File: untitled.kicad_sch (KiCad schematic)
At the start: 28 parts, among them Q1 AO3401A, Q2 AO3401A, Q3 AO3401A, U2 STM32L100RBT6A_LQFP64, U4 RC1587_3V3, U8 LTC4002ES8-4.2

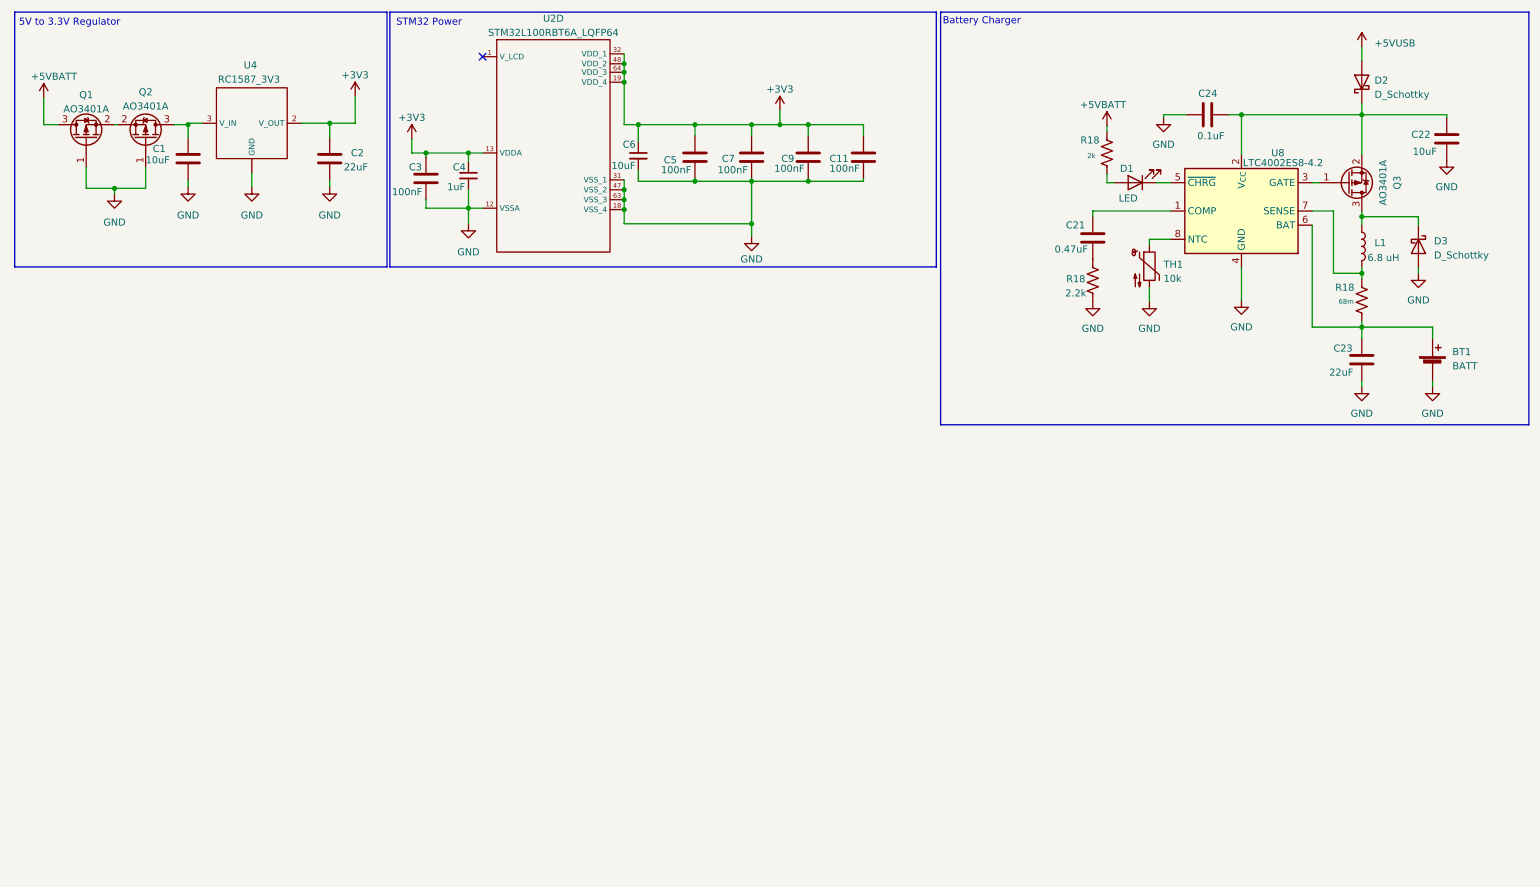
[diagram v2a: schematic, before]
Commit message: Rev 0.3
+ Updated schematic to reflect utilization of USB-B micro instead of USB-C
+ Began initial layout of PCB

- Need to look into eFuse layout, as specified layout recommendation utilizes ground pours
- Need to update SD Card footprint as pads are not linked
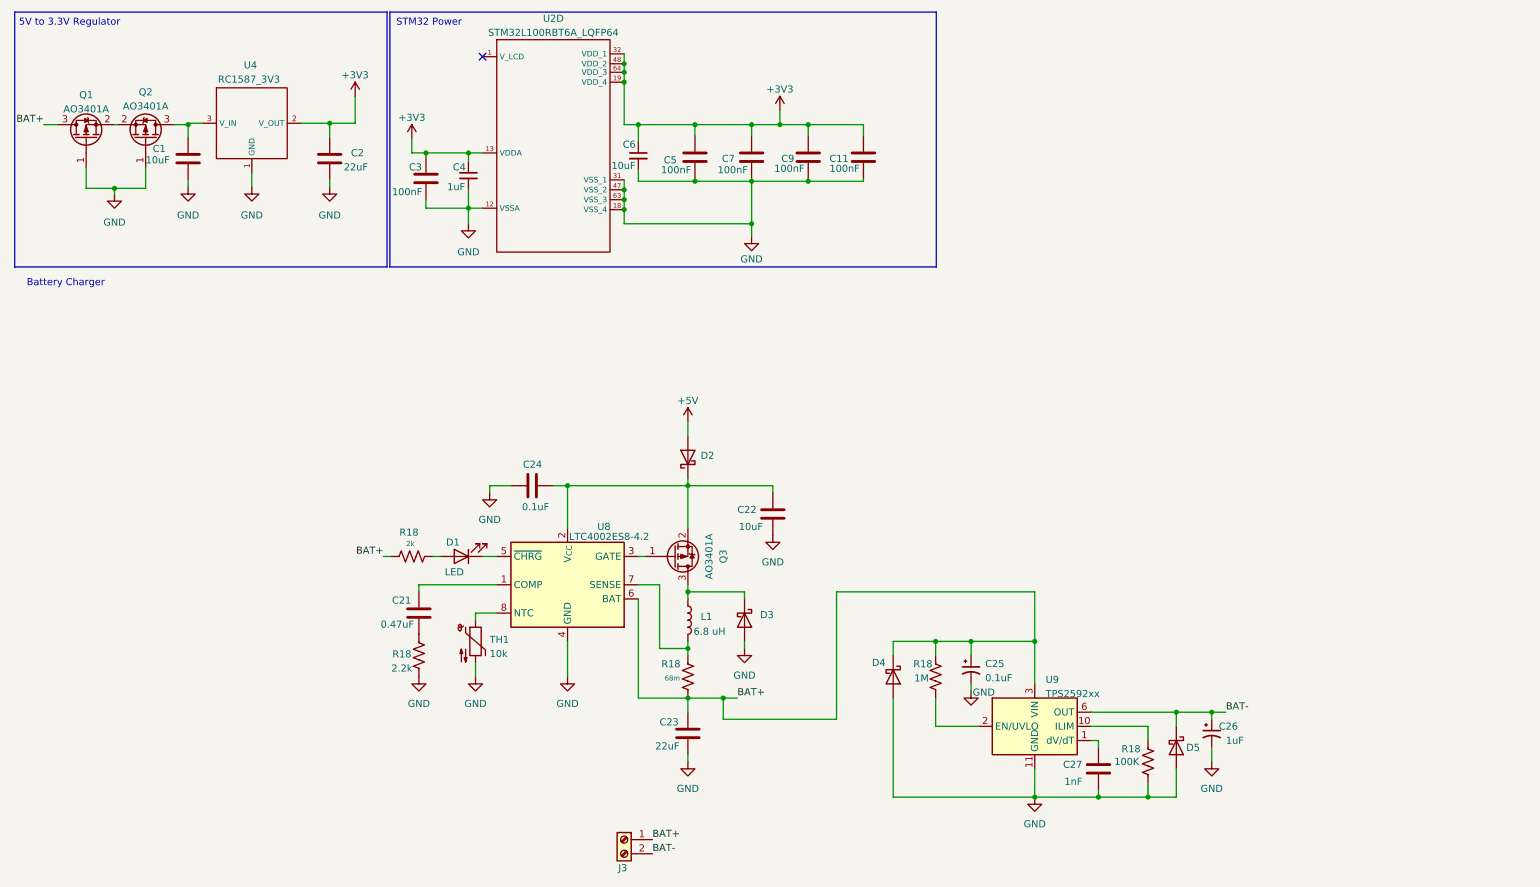
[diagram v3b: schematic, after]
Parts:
- removed BT1: BATT, symbol Device:Battery_Cell
- added C25: 0.1uF, Capacitor_SMD:C_0805_2012Metric, symbol Device:C_Polarized_Small_US
- added C26: 1uF, Capacitor_SMD:C_0805_2012Metric, symbol Device:C_Polarized_Small_US
- added C27: 1nF, Capacitor_SMD:C_0805_2012Metric, symbol Device:C
- added D4, D5: D_Schottky, Diode_SMD:D_0805_2012Metric, symbol Device:D_Schottky
- added J3: Screw_Terminal_01x02, TerminalBlock:TerminalBlock_Altech_AK300-2_P5.00mm, symbol Connector:Screw_Terminal_01x02
- added R18: 1M, Resistor_SMD:R_0805_2012Metric, symbol Device:R_US
- added R18: 100K, Resistor_SMD:R_0805_2012Metric, symbol Device:R_US
- added U9: TPS2592xx, Package_SON:VSON-10-1EP_3x3mm_P0.5mm_EP1.65x2.4mm_ThermalVias, symbol Power_Management:TPS2592xx
- D1: footprint (none) -> LED_SMD:LED_0805_2012Metric
- D2, D3: footprint (none) -> Diode_SMD:D_0805_2012Metric
- L1: footprint (none) -> Inductor_SMD:L_0805_2012Metric
- TH1: footprint (none) -> Resistor_SMD:R_0805_2012Metric
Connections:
- net +BATT is gone; now on net BAT+: R18.2
- net +5V: no longer Q1.3 (D)
- net GND: now also U4.1 (GND), C25.2, C26.2, C27.2, D4.2 (A), D5.2 (A), R18.1, U9.11 (GND); no longer U4. (GND)
- net BAT+: now reaches C23.1, R18.1, U8.6 (BAT)
- net BAT+: now also Q1.3 (D), C25.1, D4.1 (K), J3.1 (Pin_1), R18.2, U9.3 (VIN), U9.4 (VIN), U9.5 (VIN)
- new net: R18.1, U9.2 (EN/UVLO)
- new net: R18.2, U9.10 (ILIM)
- new net: C27.1, U9.1 (dV/dT)
- new net BAT-: C26.1, D5.1 (K), J3.2 (Pin_2), U9.6 (OUT), U9.7 (OUT), U9.8 (OUT)
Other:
- moved on the sheet: C21, C22, C23, C24, D1, D2, D3, L1, Q3, R18, TH1, U8

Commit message: Updated to Rev 1.1
+ Adjusted trace widths to appropriately fit IC pads while supporting wanted current and minimizing vdrop
+ Adjusted edge cuts of PCB to remove unnecessary areas
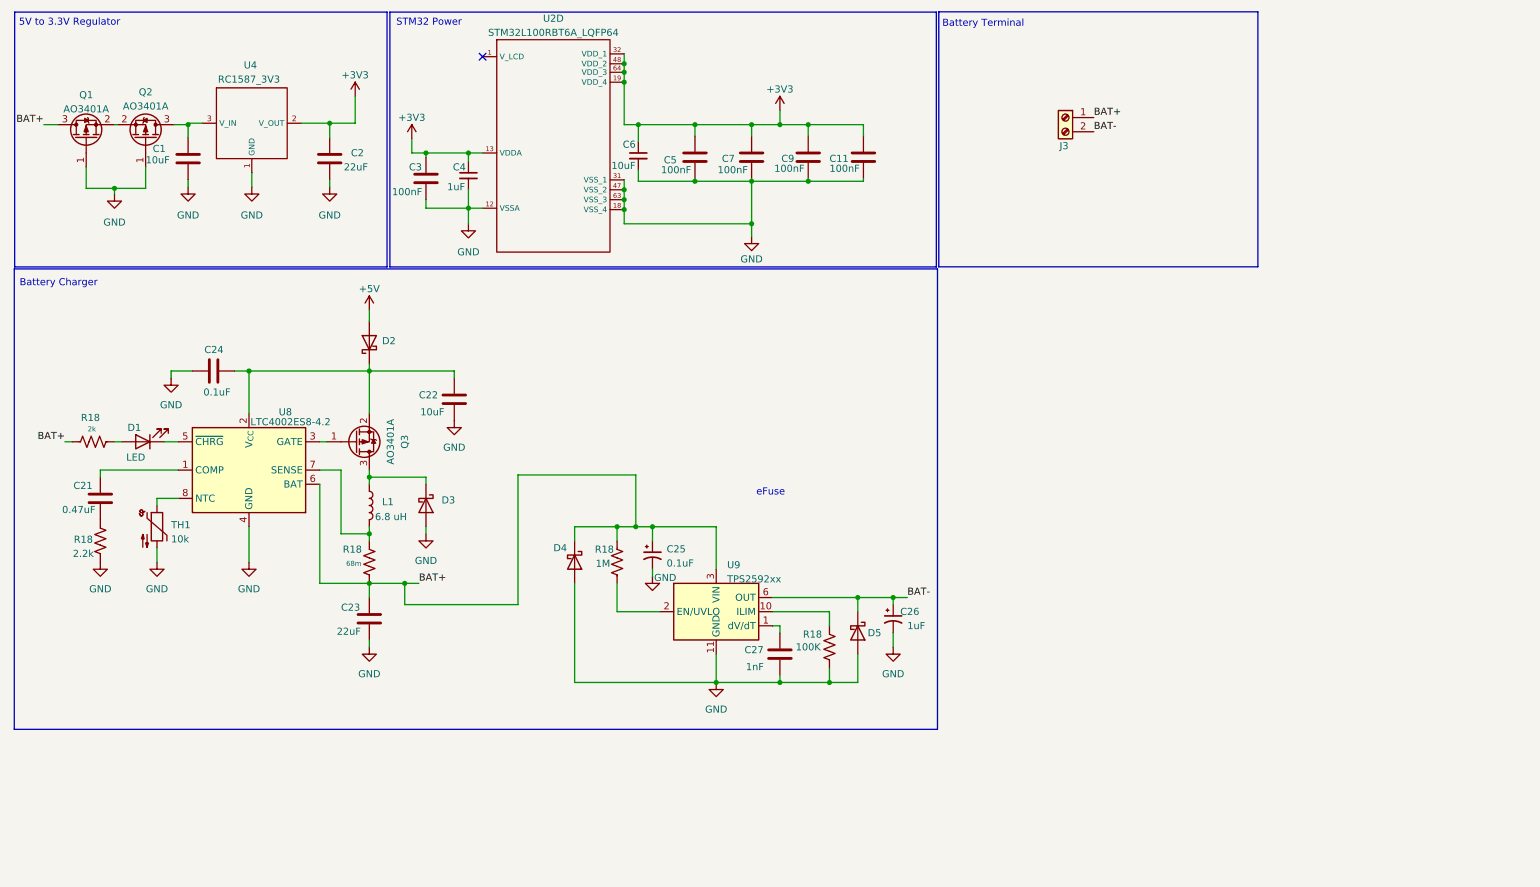
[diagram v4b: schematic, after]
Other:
- note added: "Battery Terminal"
- note added: "eFuse"
- moved on the sheet: C21, C22, C23, C24, C25, C26, C27, D1, D2, D3, D4, D5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

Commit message: Updated Rev 2.0
+ Revamped board to 4 layer with components on both signal layers (top/bottom)
+ Adjusted compactness of components, reducing size by approx 30%
+ Added mounting holes for mounting purposes
- Removed battery, batt charger, eFuse (USB driven only)
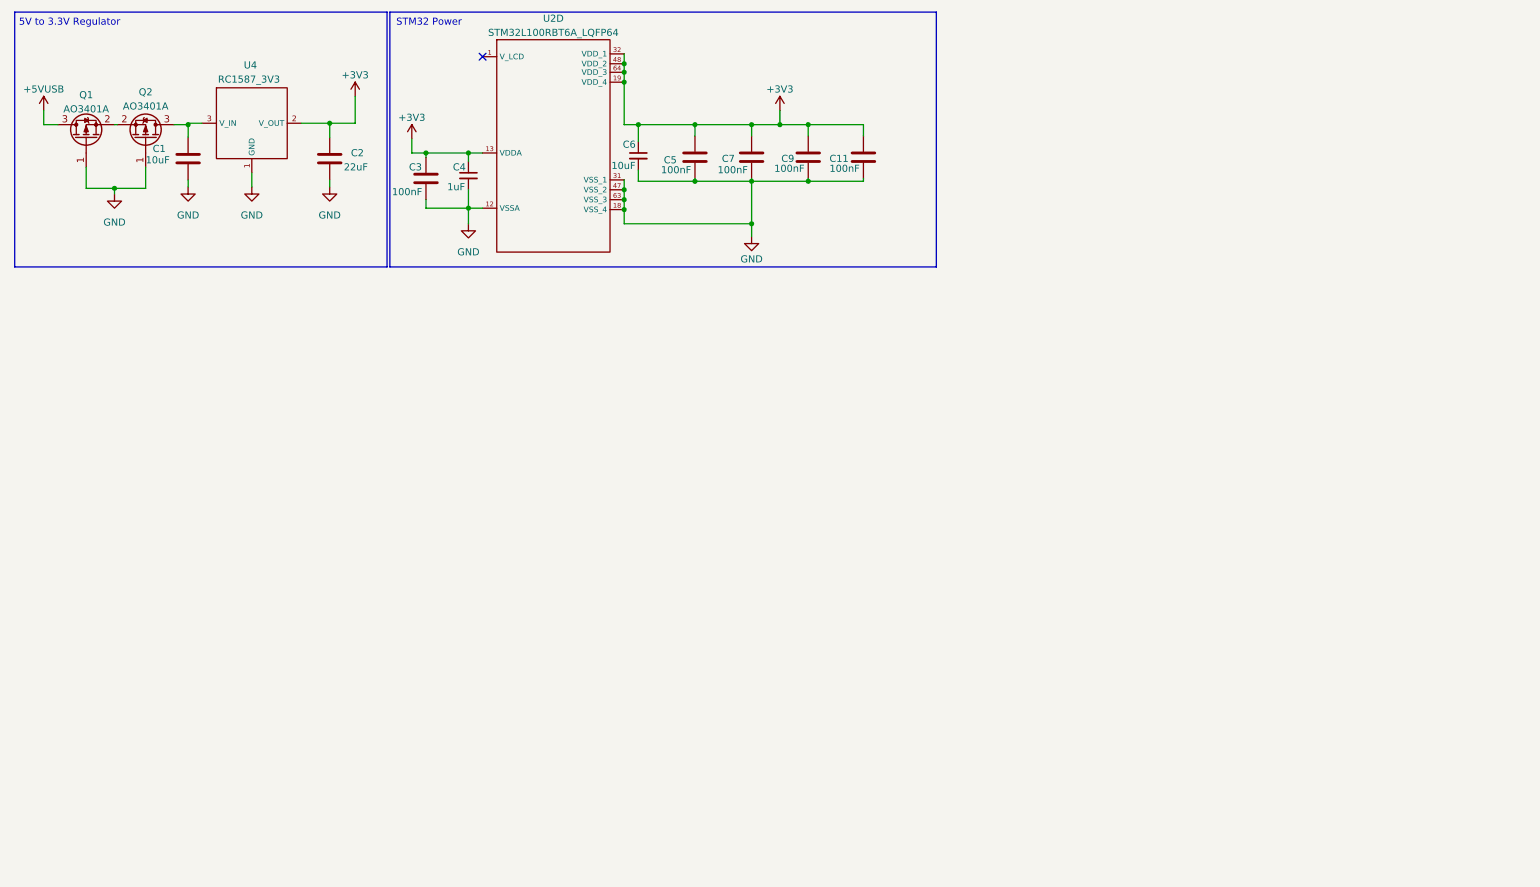
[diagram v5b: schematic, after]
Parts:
- removed C21: 0.47uF, Capacitor_SMD:C_0805_2012Metric, symbol Device:C
- removed C22: 10uF, Capacitor_SMD:C_0805_2012Metric, symbol Device:C
- removed C23: 22uF, Capacitor_SMD:C_0805_2012Metric, symbol Device:C
- removed C24: 0.1uF, Capacitor_SMD:C_0805_2012Metric, symbol Device:C
- removed C25: 0.1uF, Capacitor_SMD:C_0805_2012Metric, symbol Device:C_Polarized_Small_US
- removed C26: 1uF, Capacitor_SMD:C_0805_2012Metric, symbol Device:C_Polarized_Small_US
- removed C27: 1nF, Capacitor_SMD:C_0805_2012Metric, symbol Device:C
- removed D1: LED, LED_SMD:LED_0805_2012Metric, symbol Device:LED
- removed D2, D3, D4, D5: D_Schottky, Diode_SMD:D_0805_2012Metric, symbol Device:D_Schottky
- removed J3: Screw_Terminal_01x02, TerminalBlock:TerminalBlock_Altech_AK300-2_P5.00mm, symbol Connector:Screw_Terminal_01x02
- removed L1: 6.8 uH, Inductor_SMD:L_0805_2012Metric, symbol Device:L
- removed Q3: AO3401A, Package_TO_SOT_SMD:SOT-23, symbol Transistor_FET:AO3401A
- removed R18: 1M, Resistor_SMD:R_0805_2012Metric, symbol Device:R_US
- removed R18: 2k, Resistor_SMD:R_0805_2012Metric, symbol Device:R_US
- removed R18: 2.2k, Resistor_SMD:R_0805_2012Metric, symbol Device:R_US
- removed R18: 100K, Resistor_SMD:R_0805_2012Metric, symbol Device:R_US
- removed R18: 68m, Resistor_SMD:R_0805_2012Metric, symbol Device:R_US
- removed TH1: 10k, Resistor_SMD:R_0805_2012Metric, symbol Device:Thermistor_NTC
- removed U8: LTC4002ES8-4.2, Package_SO:SOIC-8_3.9x4.9mm_P1.27mm, symbol Battery_Management:LTC4002ES8-4.2
- removed U9: TPS2592xx, Package_SON:VSON-10-1EP_3x3mm_P0.5mm_EP1.65x2.4mm_ThermalVias, symbol Power_Management:TPS2592xx
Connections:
- net BAT+ is gone; now on net +5V: Q1.3 (D)
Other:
- note removed: "Battery Charger"
- note removed: "Battery Terminal"
- note removed: "eFuse"

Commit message: Updated to Rev B
+ Added ESD protection on USB side
+ Redesigned board layout to a SIG/GND/GND/SIG stack up and using L4 as 3V3 plane
+ Resized capacitors and resistors to 0402
+ Added 3D models of certain components
+ Added ferrite bead to 5V line
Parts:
- C1, C2, C4, C6: footprint Capacitor_SMD:C_0805_2012Metric -> Capacitor_SMD:C_0603_1608Metric
- C11, C3, C5, C7, C9: footprint Capacitor_SMD:C_0805_2012Metric -> Capacitor_SMD:C_0402_1005Metric
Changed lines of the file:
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@@
       (effects (font (size 1.27 1.27)) (justify left))
     )
-    (property "Footprint" "Capacitor_SMD:C_0805_2012Metric" (at 145.7452 42.672 0)
+    (property "Footprint" "Capacitor_SMD:C_0402_1005Metric" (at 145.7452 42.672 0)
       (effects (font (size 1.27 1.27)) hide)
     )
@@
       (effects (font (size 1.27 1.27)) (justify left))
     )
-    (property "Footprint" "Capacitor_SMD:C_0805_2012Metric" (at 155.9052 42.672 0)
+    (property "Footprint" "Capacitor_SMD:C_0402_1005Metric" (at 155.9052 42.672 0)
       (effects (font (size 1.27 1.27)) hide)
     )
@@
       (effects (font (size 1.27 1.27)) (justify left))
     )
-    (property "Footprint" "Capacitor_SMD:C_0805_2012Metric" (at 135.5852 42.672 0)
+    (property "Footprint" "Capacitor_SMD:C_0402_1005Metric" (at 135.5852 42.672 0)
       (effects (font (size 1.27 1.27)) hide)
     )
@@
       (effects (font (size 1.27 1.27)) (justify left))
     )
-    (property "Footprint" "Capacitor_SMD:C_0805_2012Metric" (at 165.8112 42.672 0)
+    (property "Footprint" "Capacitor_SMD:C_0402_1005Metric" (at 165.8112 42.672 0)
       (effects (font (size 1.27 1.27)) hide)
     )
@@
       (effects (font (size 1.27 1.27)) (justify left))
     )
-    (property "Footprint" "Capacitor_SMD:C_0805_2012Metric" (at 87.3252 46.482 0)
+    (property "Footprint" "Capacitor_SMD:C_0402_1005Metric" (at 87.3252 46.482 0)
       (effects (font (size 1.27 1.27)) hide)
     )
@@
       (effects (font (size 1.27 1.27)) (justify left))
     )
-    (property "Footprint" "Capacitor_SMD:C_0805_2012Metric" (at 70.0532 42.926 0)
+    (property "Footprint" "Capacitor_SMD:C_0603_1608Metric" (at 70.0532 42.926 0)
       (effects (font (size 1.27 1.27)) hide)
     )
@@
       (effects (font (size 1.27 1.27)) (justify left))
     )
-    (property "Footprint" "Capacitor_SMD:C_0805_2012Metric" (at 44.6532 42.926 0)
+    (property "Footprint" "Capacitor_SMD:C_0603_1608Metric" (at 44.6532 42.926 0)
       (effects (font (size 1.27 1.27)) hide)
     )
@@
       (effects (font (size 1.27 1.27)) (justify left))
     )
-    (property "Footprint" "Capacitor_SMD:C_0805_2012Metric" (at 124.46 38.608 0)
+    (property "Footprint" "Capacitor_SMD:C_0603_1608Metric" (at 124.46 38.608 0)
       (effects (font (size 1.27 1.27)) hide)
     )
@@
       (effects (font (size 1.27 1.27)) (justify left))
     )
-    (property "Footprint" "Capacitor_SMD:C_0805_2012Metric" (at 93.98 42.164 0)
-      (effects (font (size 1.27 1.27)) hide)
-    )
+    (property "Footprint" "Capacitor_SMD:C_0603_1608Metric" (at 93.98 42.164 0)
+      (effects (font (size 1.27 1.27)) hide)
+    )
